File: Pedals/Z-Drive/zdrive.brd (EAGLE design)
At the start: 55.9 x 54.6 mm, 30 parts, among them IC1 MC1458P, Q1 2N7000, Q2 2N7000

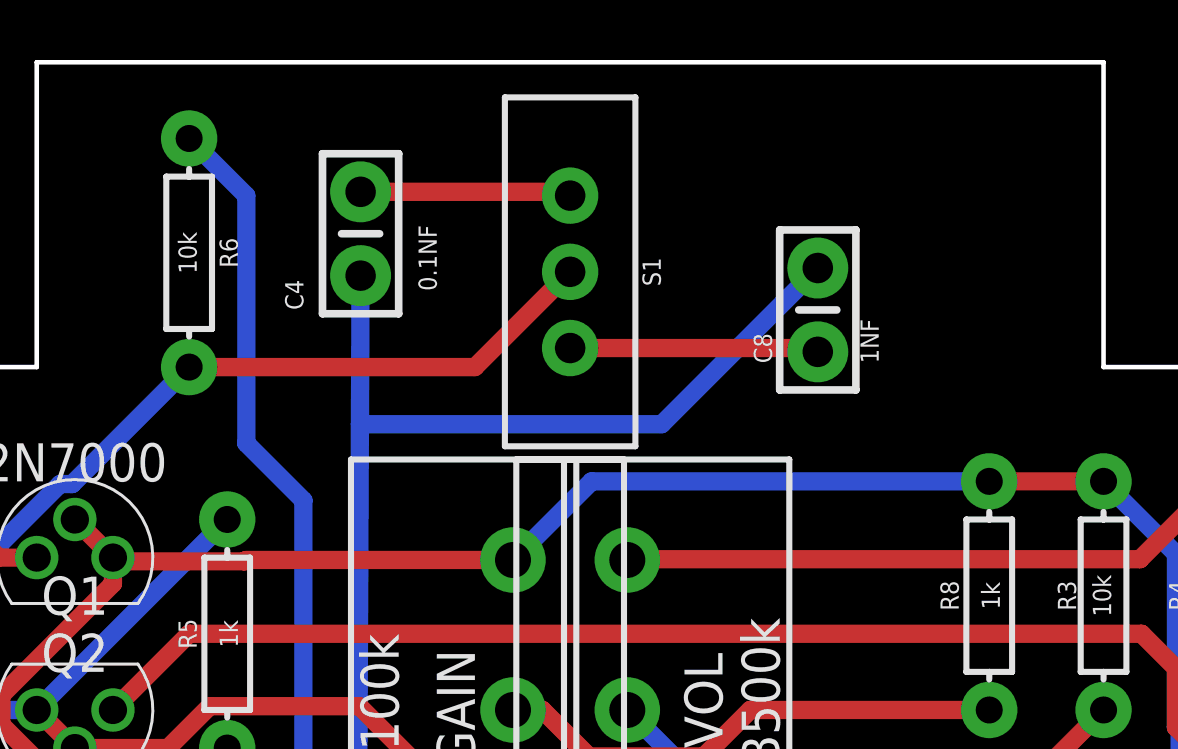
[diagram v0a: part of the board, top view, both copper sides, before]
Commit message: Update switch to correct footprint size
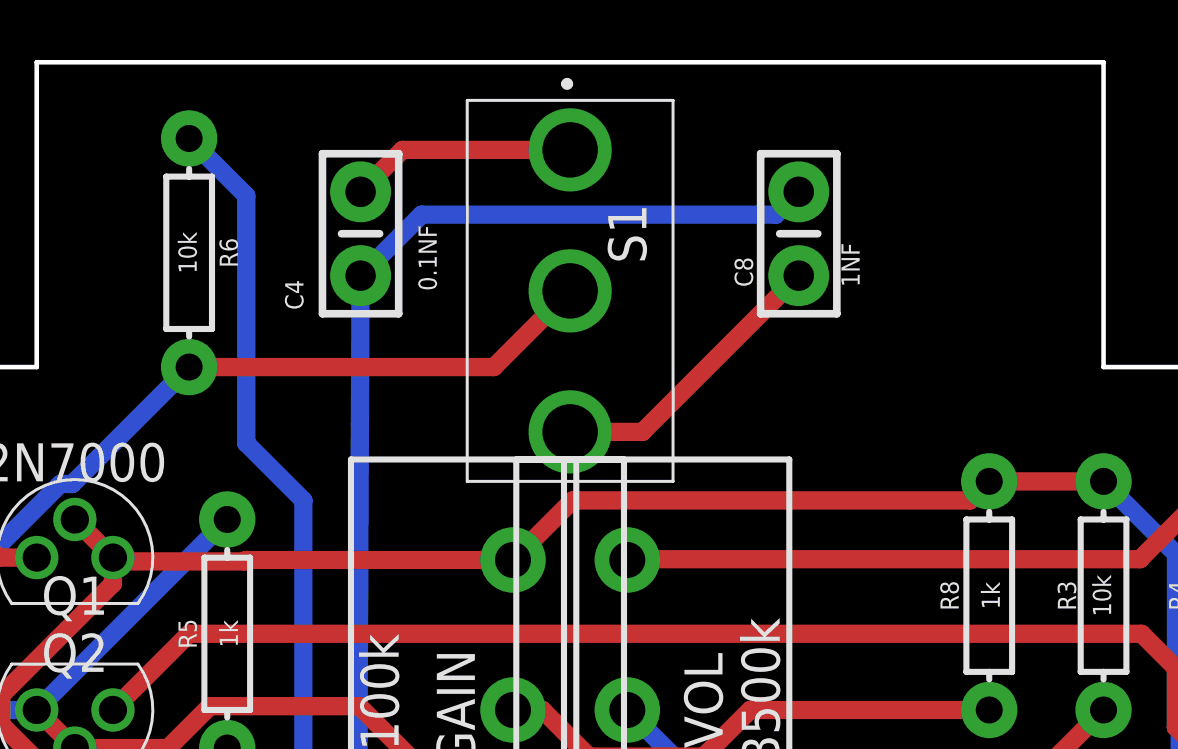
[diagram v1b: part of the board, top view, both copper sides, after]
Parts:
- S1: value (none) -> 100SP1T1B2M2QE; device SparkFun-Switches:SWITCH_SPDT_PTH_11.6X4.0MM -> SamacSys_Parts:100SP1T1B4M2QE
- moved C8 2.62 mm to (35.6, 48.9)
- moved S1 0.63 mm to (27.9, 47.0), turned to 270 degrees
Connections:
- net N$11: now also S1.1; no longer S1.3
- net N$12: now also S1.3; no longer S1.1
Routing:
- net N$7: track 56.8 -> 55.2 mm
- net N$12: track 8.31 -> 9.78 mm
- net N$11: track 7.04 -> 7.56 mm
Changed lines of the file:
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@@
 <attribute name="VALUE" x="43.18" y="1.651" size="0.6096" layer="25" font="vector" ratio="20" align="top-center"/>
 </element>
-<element name="C8" library="Custom-Parts" package="CAP-PTH-SMALL-KIT" value="1NF" x="36.195" y="46.355" smashed="yes" rot="R90">
-<attribute name="NAME" x="34.671" y="44.577" size="0.6096" layer="25" rot="R90"/>
-<attribute name="VALUE" x="38.227" y="44.577" size="0.6096" layer="25" rot="R90"/>
+<element name="C8" library="Custom-Parts" package="CAP-PTH-SMALL-KIT" value="1NF" x="35.56" y="48.895" smashed="yes" rot="R90">
+<attribute name="NAME" x="34.036" y="47.117" size="0.6096" layer="25" rot="R90"/>
+<attribute name="VALUE" x="37.592" y="47.117" size="0.6096" layer="25" rot="R90"/>
 </element>
 <element name="D1" library="SparkFun-DiscreteSemi" library_urn="urn:adsk.eagle:library:514" package="DIODE-1N4001-KIT" package3d_urn="urn:adsk.eagle:package:38455/1" value="BAT41" x="6.35" y="35.56" smashed="yes" rot="R90">
@@
 <attribute name="VALUE" x="41.656" y="36.83" size="0.6096" layer="25" font="vector" ratio="20" rot="R90" align="top-center"/>
 </element>
-<element name="S1" library="SparkFun-Switches" library_urn="urn:adsk.eagle:library:535" package="SWITCH_SPDT_PTH_11.6X4.0MM" package3d_urn="urn:adsk.eagle:package:40177/1" value="" x="27.94" y="47.625" smashed="yes" rot="R180">
-<attribute name="NAME" x="30.353" y="47.625" size="0.6096" layer="25" font="vector" ratio="20" rot="R270" align="bottom-center"/>
-<attribute name="PROD_ID" value="SWCH-08261" x="12.7" y="53.975" size="1.778" layer="27" rot="R180" display="off"/>
-<attribute name="SF_SKU" value="COM-00102" x="12.7" y="53.975" size="1.778" layer="27" rot="R180" display="off"/>
-<attribute name="VALUE" x="25.527" y="47.625" size="0.6096" layer="27" font="vector" ratio="20" rot="R270" align="top-center"/>
-</element>
 <element name="TONE" library="Custom-Parts" package="3RP/1610N" package3d_urn="urn:adsk.eagle:package:22726/1" value="B50k" x="29.845" y="15.24" smashed="yes" rot="R270">
 <attribute name="NAME" x="33.655" y="17.145" size="1.27" layer="25" rot="R270"/>
@@
 <attribute name="POPULARITY" value="8" x="13.335" y="-6.35" size="1.778" layer="27" rot="R270" display="off"/>
 <attribute name="VALUE" x="20.955" y="35.56" size="1.27" layer="25" rot="R270"/>
+</element>
+<element name="S1" library="SamacSys_Parts" package="100SP1T1B4M2QE" value="100SP1T1B2M2QE" x="27.94" y="46.99" smashed="yes" rot="R270">
+<attribute name="DESCRIPTION" value="Toggle Switches 5A 120VAC/28VDC On-None-On PC Mnt" x="27.94" y="46.99" size="1.778" layer="27" rot="R270" display="off"/>
+<attribute name="HEIGHT" value="28mm" x="27.94" y="46.99" size="1.778" layer="27" rot="R270" display="off"/>
+<attribute name="MANUFACTURER_NAME" value="E-Switch" x="27.94" y="46.99" size="1.778" layer="27" rot="R270" display="off"/>
+<attribute name="MANUFACTURER_PART_NUMBER" value="100SP1T1B2M2QE" x="27.94" y="46.99" size="1.778" layer="27" rot="R270" display="off"/>
+<attribute name="MOUSER_PART_NUMBER" value="612-100SP1T1B2M2QE" x="27.94" y="46.99" size="1.778" layer="27" rot="R270" display="off"/>
+<attribute name="MOUSER_PRICE-STOCK" value="https://www.mouser.co.uk/ProductDetail/E-Switch/100SP1T1B2M2QE?qs=f57gQzlyLipVPLzNFzaEDQ%3D%3D" x="27.94" y="46.99" size="1.778" layer="27" rot="R270" display="off"/>
+<attribute name="NAME" x="29.845" y="48.895" size="1.27" layer="25" rot="R270" align="center"/>
 </element>
 </elements>
@@
 <wire x1="12.7" y1="38.1" x2="12.827" y2="37.973" width="0.6096" layer="1"/>
 <wire x1="12.827" y1="37.973" x2="17.0886625" y2="37.973" width="0.6096" layer="1"/>
-<wire x1="26.035" y1="38.02" x2="28.655" y2="40.64" width="0.6096" layer="16"/>
-<wire x1="28.655" y1="40.64" x2="41.91" y2="40.64" width="0.6096" layer="16"/>
 <wire x1="48.133" y1="32.4413375" x2="48.26" y2="32.3143375" width="0.6096" layer="16"/>
 <wire x1="48.26" y1="32.3143375" x2="48.26" y2="29.337" width="0.6096" layer="16"/>
@@
 <wire x1="48.26" y1="29.337" x2="46.7868" y2="27.8638" width="0.6096" layer="16"/>
 <wire x1="46.7868" y1="27.8638" x2="46.7868" y2="25.932775" width="0.6096" layer="16"/>
+<wire x1="26.035" y1="38.02" x2="28.02" y2="40.005" width="0.6096" layer="1"/>
+<wire x1="41.275" y1="40.005" x2="41.91" y2="40.64" width="0.6096" layer="1"/>
+<wire x1="28.02" y1="40.005" x2="41.275" y2="40.005" width="0.6096" layer="1"/>
 </signal>
 <signal name="N$1">
@@
 <contactref element="C7" pad="1"/>
 <contactref element="R2" pad="P$2"/>
-<contactref element="S1" pad="2"/>
 <wire x1="2.54" y1="29.21" x2="2.54" y2="26.67" width="0.6096" layer="1"/>
 <wire x1="4.2672" y1="9.89516875" x2="12.76536875" y2="1.397" width="0.6096" layer="16"/>
@@
 <wire x1="2.54" y1="26.67" x2="4.2672" y2="24.9428" width="0.6096" layer="16"/>
 <wire x1="4.2672" y1="24.9428" x2="4.2672" y2="9.89516875" width="0.6096" layer="16"/>
-<wire x1="24.765" y1="44.45" x2="27.94" y2="47.625" width="0.6096" layer="1"/>
-<wire x1="15.24" y1="44.45" x2="24.765" y2="44.45" width="0.6096" layer="1"/>
+<contactref element="S1" pad="2"/>
+<wire x1="15.24" y1="44.45" x2="25.4" y2="44.45" width="0.6096" layer="1"/>
+<wire x1="25.4" y1="44.45" x2="27.94" y2="46.99" width="0.6096" layer="1"/>
 </signal>
 <signal name="N$6">
@@
 <wire x1="20.932790625" y1="42.5451" x2="20.83366875" y2="20.44133125" width="0.6096" layer="16"/>
 <wire x1="20.83366875" y1="20.44133125" x2="26.035" y2="15.24" width="0.6096" layer="16"/>
-<wire x1="20.932790625" y1="42.5451" x2="30.9881" y2="42.5451" width="0.6096" layer="16"/>
-<wire x1="30.9881" y1="42.5451" x2="36.195" y2="47.752" width="0.6096" layer="16"/>
+<wire x1="20.955" y1="47.498" x2="22.987" y2="49.53" width="0.6096" layer="16"/>
+<wire x1="34.798" y1="49.53" x2="35.56" y2="50.292" width="0.6096" layer="16"/>
+<wire x1="22.987" y1="49.53" x2="34.798" y2="49.53" width="0.6096" layer="16"/>
 </signal>
 <signal name="N$8">
@@
 </signal>
 <signal name="N$11">
+<contactref element="C4" pad="1"/>
+<contactref element="S1" pad="1"/>
+<wire x1="20.955" y1="50.292" x2="22.353" y2="51.69" width="0.6096" layer="1"/>
+<wire x1="22.353" y1="51.69" x2="27.94" y2="51.69" width="0.6096" layer="1"/>
+</signal>
+<signal name="N$12">
+<contactref element="C8" pad="1"/>
 <contactref element="S1" pad="3"/>
-<contactref element="C4" pad="1"/>
-<wire x1="20.955" y1="50.292" x2="27.813" y2="50.292" width="0.6096" layer="1"/>
-<wire x1="27.813" y1="50.292" x2="27.94" y2="50.165" width="0.6096" layer="1"/>
-</signal>
-<signal name="N$12">
-<contactref element="S1" pad="1"/>
-<contactref element="C8" pad="1"/>
-<wire x1="27.94" y1="45.085" x2="36.068" y2="45.085" width="0.6096" layer="1"/>
-<wire x1="36.068" y1="45.085" x2="36.195" y2="44.958" width="0.6096" layer="1"/>
+<wire x1="35.56" y1="47.498" x2="30.352" y2="42.29" width="0.6096" layer="1"/>
+<wire x1="30.352" y1="42.29" x2="27.94" y2="42.29" width="0.6096" layer="1"/>
 </signal>
 </signals>

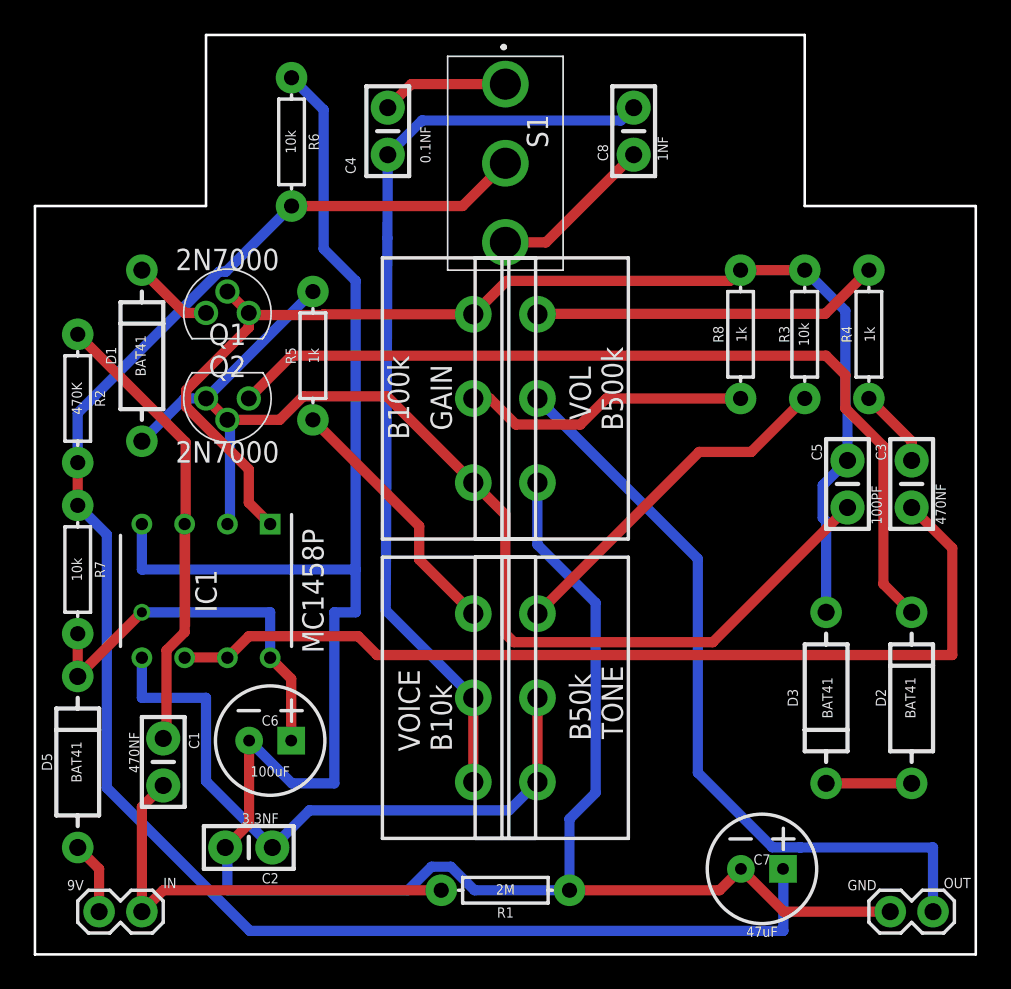
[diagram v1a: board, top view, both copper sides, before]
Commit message: Switch pots to bottom and add gnd plane
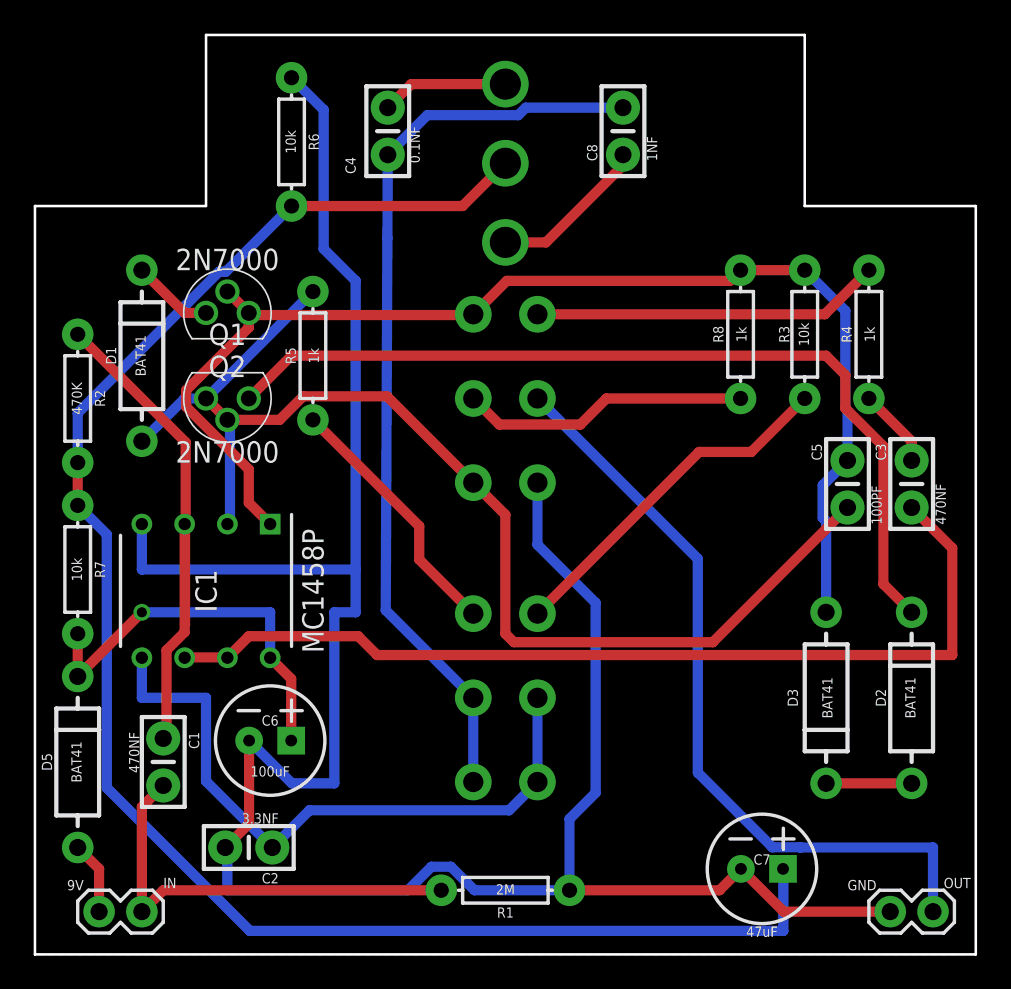
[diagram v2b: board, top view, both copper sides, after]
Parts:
- moved C8 0.64 mm to (34.9, 48.9)
- flipped GAIN to the bottom
- flipped S1 to the bottom
- flipped TONE to the bottom
- flipped VOICE to the bottom
- flipped VOL to the bottom
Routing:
- net N$7: track 55.2 -> 54.5 mm
- added copper zone on layer 1, net GND
- added copper zone on layer 16, net GND

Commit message: Flip top pots
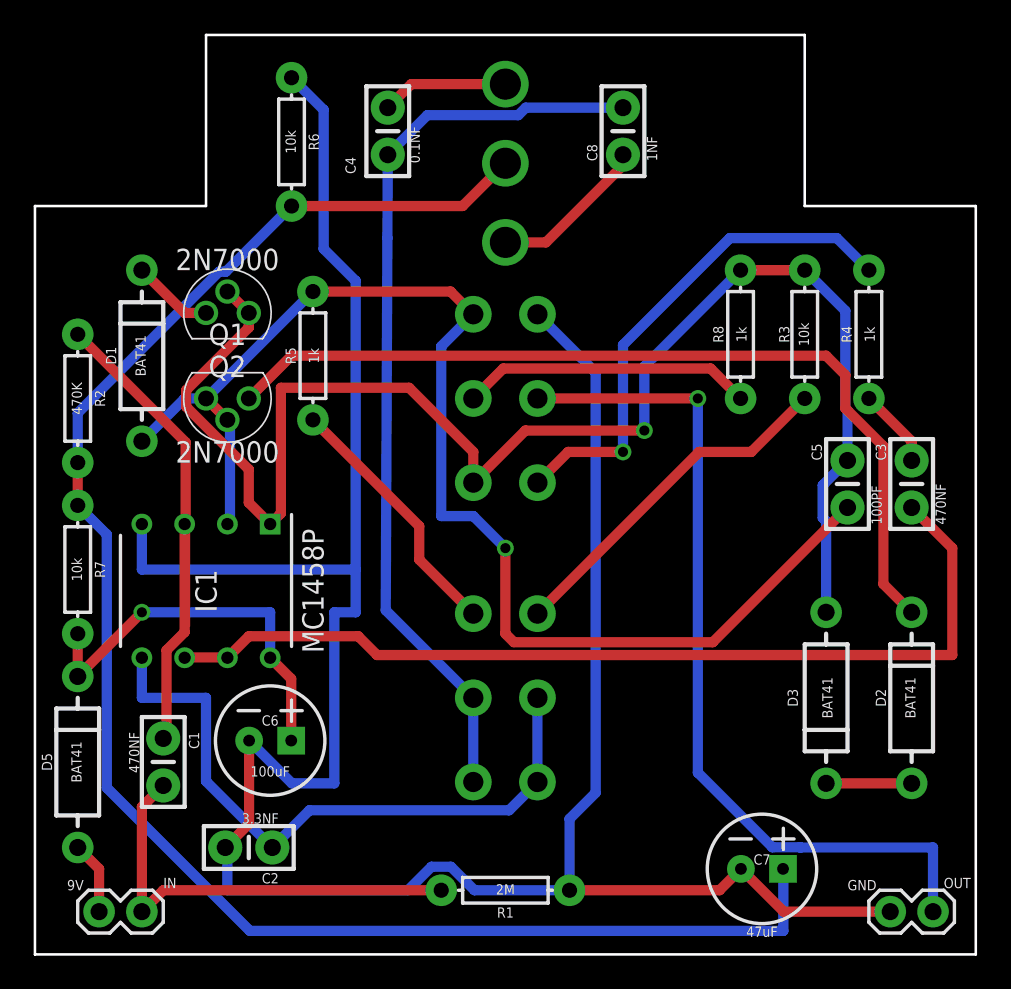
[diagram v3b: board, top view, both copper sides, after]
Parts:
- turned GAIN to 270 degrees
- turned VOL to 90 degrees
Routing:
- net OP1: track 74.2 -> 90.3 mm, vias 0 -> 1
- net GND: track 144.2 -> 154.2 mm
- net N$4: track 20.8 -> 30.2 mm, vias 0 -> 1
- net OUT: track 45.8 -> 51.4 mm, vias 0 -> 1
- net OP2: track 72.9 -> 78.4 mm, vias 0 -> 1
- removed copper zone on layer 1, net GND
- removed copper zone on layer 16, net GND
